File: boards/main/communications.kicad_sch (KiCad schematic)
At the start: 14 parts, among them IC1 Wio-SX1262, J5 IPEX, U8 MAX-M10S-00B

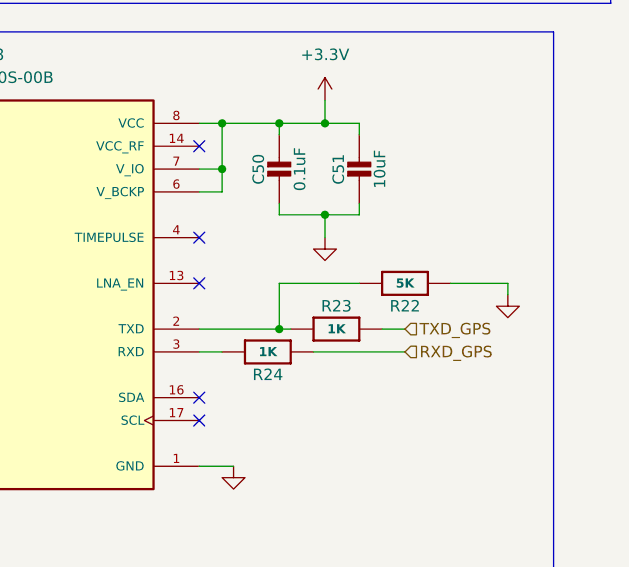
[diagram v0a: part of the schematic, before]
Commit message: Board migrations. Move to newer LED and IMU
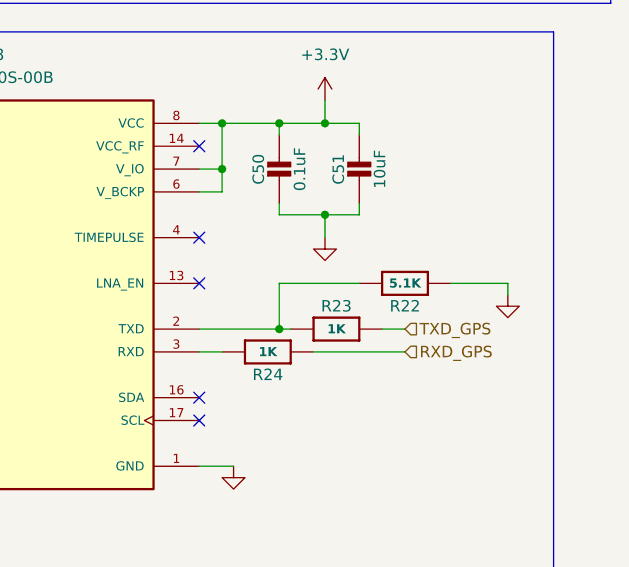
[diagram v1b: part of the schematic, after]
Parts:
- AE1: DigiKey_PN (none) -> 712-1575AT43A0040001ECT-ND; MPN 1575AT43A0040E -> 1575AT43A0040001E; Manufacturer (none) -> Johanson Technology Inc.; Sourcing_Note (none) -> MPN corrected: '1575AT43A0040E' is not an orderable Johanso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
- C50: Dielectric (none) -> X7R; DigiKey_PN (none) -> 1276-6844-1-ND; MPN 0402B104K160HI -> CL05B104KO5VPNC; Manufacturer (none) -> Samsung Electro-Mechanics; Voltage (none) -> 16V
- C51: Dielectric (none) -> X5R; DigiKey_PN (none) -> 1276-6456-1-ND; Manufacturer (none) -> Samsung Electro-Mechanics; Voltage (none) -> 10V
- C52, C53: MPN (none) -> DNP; Sourcing_Note (none) -> Not mounted - GNSS RF matching option, leave unpopulated un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
- D23: DigiKey_PN (none) -> 296-39341-1-ND; Manufacturer (none) -> Texas Instruments
- IC1: DigiKey_PN (none) -> 1597-114993390CT-ND; Manufacturer (none) -> Seeed Technology Co., Ltd
- J5: DigiKey_PN (none) -> 931-1157-1-ND; Manufacturer (none) -> Taoglas Limited
- R21: MPN (none) -> DNP; Sourcing_Note (none) -> Not mounted - GNSS RF matching option.
- R22: value 5K -> 5.1K; DigiKey_PN (none) -> 311-5.10KHRCT-ND; MPN RT0603BRE075KL -> RC0603FR-075K1L; Manufacturer (none) -> YAGEO; Tolerance (none) -> 1%
- R23, R24: Manufacturer (none) -> YAGEO; Tolerance (none) -> 1%
- R25: DigiKey_PN (none) -> 311-0.0GRCT-ND; MPN RT0603BRE075KL -> RC0603JR-070RL; Manufacturer (none) -> YAGEO; Sourcing_Note (none) -> MPN corrected: this 0R jumper previously carried RT0603BRE0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; Tolerance (none) -> Jumper
- U8: DigiKey_PN (none) -> 672-MAX-M10S-00BCT-ND; Manufacturer (none) -> u-blox

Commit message: some more component reworking. Moved to 10 lane ribbon connects between all boards
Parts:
- added C54: 10uF, Capacitor_SMD:C_0805_2012Metric, symbol smart_compass_main:CAP_CERAMIC0805-NOOUTLINE
- AE1: symbol 2026-06-05_23-02-22:1575AT43A0040E -> smart_compass_main:1575AT43A0040E
- C50, C51, C52, C53: symbol Adafruit ESP32-S3 8MB No PSRAM-eagle-import:CAP_CERAMIC0805-NOOUTLINE -> smart_compass_main:CAP_CERAMIC0805-NOOUTLINE
- D23: symbol TPD1E05U06DPYR:TPD1E05U06DPYR -> smart_compass_main:TPD1E05U06DPYR
- IC1: symbol 114993390:114993390 -> smart_compass_main:114993390
- J5: symbol RECE_20369_001E_01:RECE.20369.001E.01 -> smart_compass_main:RECE.20369.001E.01
- R21, R23, R24, R25: symbol Adafruit ESP32-S3 8MB No PSRAM-eagle-import:RESISTOR_0603_NOOUT -> smart_compass_main:RESISTOR_0603_NOOUT
- R22: value 5.1K -> 100K; symbol Adafruit ESP32-S3 8MB No PSRAM-eagle-import:RESISTOR_0603_NOOUT -> smart_compass_main:RESISTOR_0603_NOOUT; MPN RC0603FR-075K1L -> RC0603FR-07100KL
- U8: symbol MAX-M10S-00B:MAX-M10S-00B -> smart_compass_main:MAX-M10S-00B
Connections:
- net +3.3V: now also C54.1
- net GND: now also C54.2

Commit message: Add a voltage booster and logic shift to the LED ring. Power consumption implications, but necessary
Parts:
- AE1: footprint 1575AT43A0040E:ANT_1575AT_JOT -> (none)
- D2: renamed from D23; footprint TPD1E05U06DPYR:DIO_TPD1E05U06DPYR -> (none)
- IC1: footprint 114993390:114993390 -> (none)
- J5: footprint RECE.20369:RECE20369001E01 -> (none)
- U8: footprint MAX-M10S-00B:XCVR_MAX-M10S-00B -> (none)
- renumbered C54 to C22, C50 to C23, C51 to C24, C52 to C25, C53 to C26, R21 to R18, R22 to R19, R23 to R20, R24 to R21, R25 to R22

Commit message: Update the footprint for the flash chip
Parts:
- renumbered C22 to C21, C23 to C22, C24 to C23, C25 to C24, C26 to C25

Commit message: grab a bunch of datasheets. Fix some models, fix some footprints, replace an unsuited capacitor
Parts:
- U8: MANUFACTURER u-blox -> (none)
- renumbered C21 to C22, C22 to C23, C23 to C24, C24 to C25, C25 to C26

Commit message: Fix missing/incorrect digikey numbers
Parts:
- R19: DigiKey_PN 311-5.10KHRCT-ND -> 311-100KHRCT-ND
- R20, R21: DigiKey_PN (none) -> 311-1.00KHRCT-ND
